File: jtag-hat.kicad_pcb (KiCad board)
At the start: 2 copper layers, 65 x 56 mm, 18 parts, among them J1 I2C header, J10 ARM-20 JTAG, J2 RPi_GPIO, J3 RPI UART, J4 UART IN, J5 JTAG 2x4, SW1 SW_Push

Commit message: v1.3
- Swapped the JTAG connector placements for connecting convenience
- Changed resistors to 0402
- Removed silkscreen around unused PI-header holes
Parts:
- R1, R2, R3, R4, R5: footprint Resistor_SMD:R_0805_2012Metric_Pad1.20x1.40mm_HandSolder -> Resistor_SMD:R_0402_1005Metric_Pad0.72x0.64mm_HandSolder
- moved J5 29.3 mm to (163.2, 81.4)
- moved J10 13.6 mm to (153.6, 80.0)
- moved R2 5.31 mm to (156.7, 67.0), turned to -90 degrees
- moved R5 4.57 mm to (154.4, 67.0)
- moved R3 2.38 mm to (153.7, 64.0), turned to 90 degrees
- moved R4 1.32 mm to (151.3, 64.0)
- moved G*** 0.18 mm to (113.4, 96.3)
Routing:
- net /RPi_GPIO/TRST: track 67.1 -> 50.9 mm
- net /RPi_GPIO/TDI: track 68.1 -> 53.0 mm, vias 0 -> 1
- net /RPi_GPIO/TCK: track 55.7 -> 40.9 mm
- net /RPi_GPIO/RXD5: track 4.38 -> 11.4 mm
- net /RPi_GPIO/TDO: track 48.1 -> 54.9 mm
- net /RPi_GPIO/PIN6_RXTX: track 11.6 -> 17.6 mm, vias 0 -> 2
- net /RPi_GPIO/SRST: track 30.7 -> 25.1 mm
- net /RPi_GPIO/PIN4_RXTX: track 20.0 -> 14.9 mm
- net /RPi_GPIO/TXD5: track 7.08 -> 10.9 mm
- net GND: track 118.8 -> 115.5 mm, vias 0 -> 1
- net /RPi_GPIO/TMS: track 58.5 -> 56.2 mm
- net /RPi_GPIO/GPIO23: track 71.5 -> 73.6 mm, vias 0 -> 1
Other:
- board text added: "JTAG HAT + Shutdown v1.3"
- board text removed: "JTAG HAT + Shutdown v1.2"

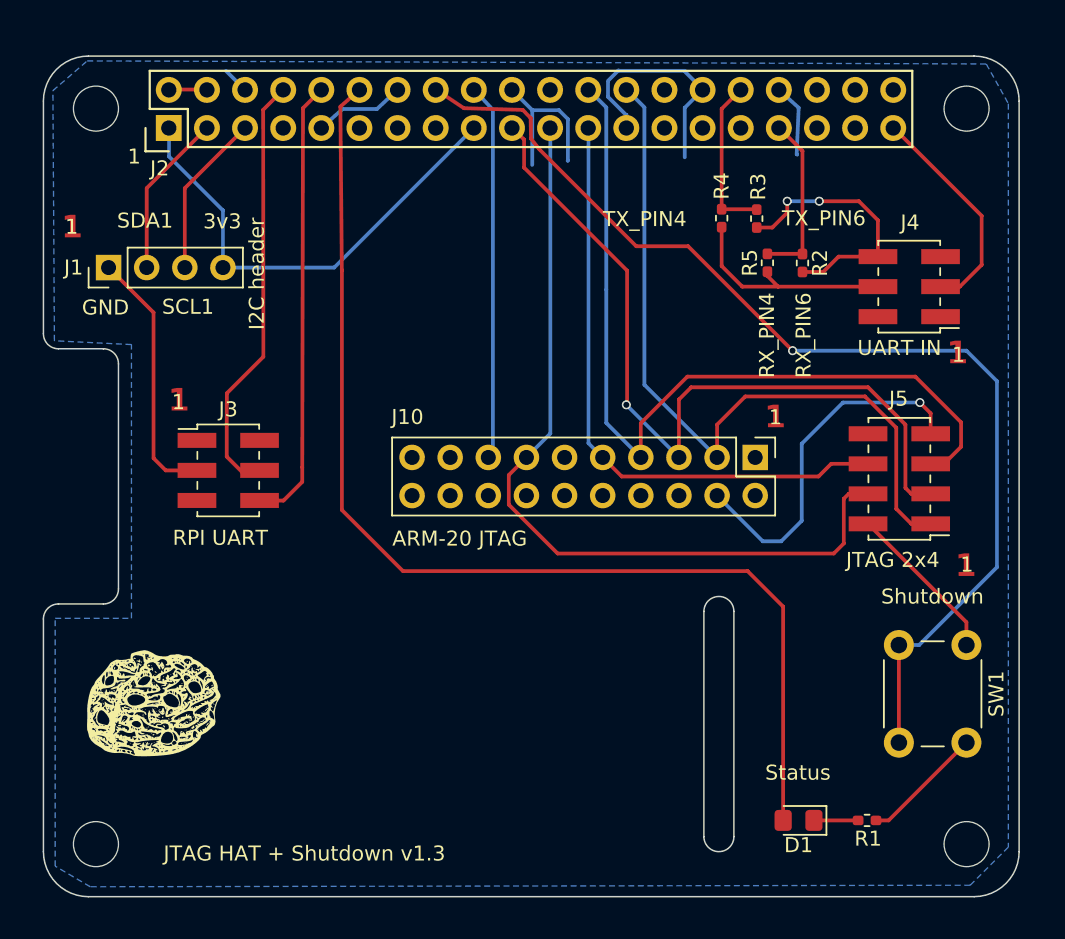
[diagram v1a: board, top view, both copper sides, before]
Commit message: v1.4
    - Rotate rpi uart header
    - Add second status led
    - Minor cleanup
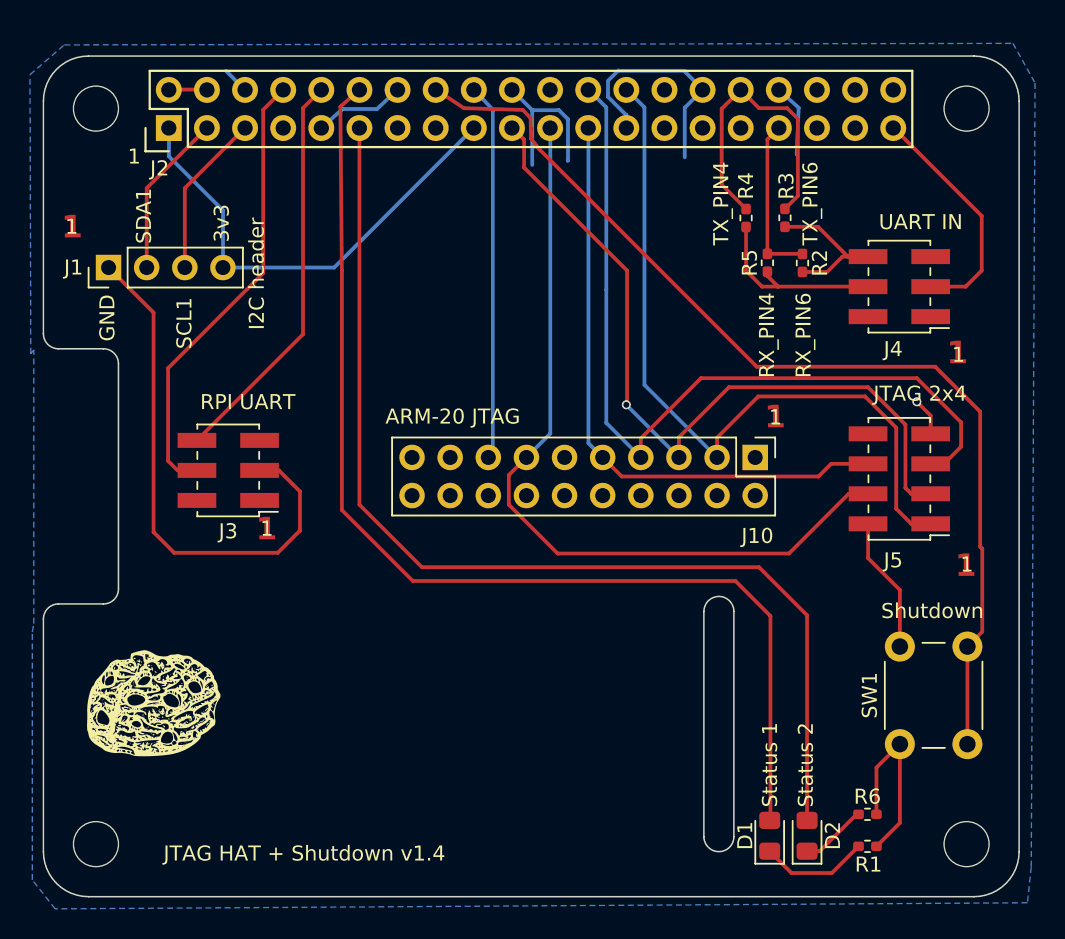
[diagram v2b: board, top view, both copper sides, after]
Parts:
- added D2: LED, LED_SMD:LED_0805_2012Metric_Pad1.15x1.40mm_HandSolder, F.Cu at (157.0, 105.2)
- added R6: R2200, Resistor_SMD:R_0402_1005Metric_Pad0.72x0.64mm_HandSolder, F.Cu at (161.0, 103.7)
- moved SW1 7.95 mm to (163.2, 99.1), turned to 90 degrees
- moved D1 2.18 mm to (154.5, 105.2), turned to 90 degrees
- moved R3 1.88 mm to (155.5, 64.0)
- moved R1 1.73 mm to (161.0, 105.9)
- moved R4 1.63 mm to (153.0, 64.0)
- moved J4 0.66 mm to (163.2, 68.6)
- turned J3 to 180 degrees
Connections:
- J2 pad 11: unconnected-(J2-BCM17-Pad11) -> /RPi_GPIO/GPIO17
- J5 pad 8: unconnected-(J5-Pin_8-Pad8) -> /RPi_GPIO/VCC-NC
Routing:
- net /RPi_GPIO/GPIO17: track 0.00 -> 71.6 mm
- net /RPi_GPIO/TXD5: track 10.9 -> 20.1 mm
- net /RPi_GPIO/PIN6_RXTX: track 17.6 -> 11.2 mm, vias 2 -> 0
- net /RPi_GPIO/GPIO23: track 73.6 -> 68.4 mm, vias 1 -> 0
- net Net-(D2-K): track 0.00 -> 4.45 mm
- net Net-(D1-K): track 2.94 -> 7.26 mm
- net /RPi_GPIO/RXD0: track 29.9 -> 26.8 mm
- net /RPi_GPIO/PIN4_RXTX: track 14.9 -> 12.8 mm
- net /RPi_GPIO/TDO: track 54.9 -> 53.2 mm
- net /RPi_GPIO/TXD0: track 28.6 -> 30.1 mm
- net /RPi_GPIO/TDI: track 53.0 -> 51.5 mm
- net /RPi_GPIO/GPIO18: track 74.9 -> 73.7 mm
- net /RPi_GPIO/TMS: track 56.2 -> 55.6 mm
- net /RPi_GPIO/TRST: track 50.9 -> 50.4 mm
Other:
- board text added: "JTAG HAT + Shutdown v1.4"
- board text added: "Status 1"
- board text added: "Status 2"
- board text removed: "JTAG HAT + Shutdown v1.3"
- board text removed: "Status"

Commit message: v1.5
- Changed mounting holes to 3.2mm (for M3)
- Swapped Pi-header for a straight pin-header
- Converted schematic from sub-schematic
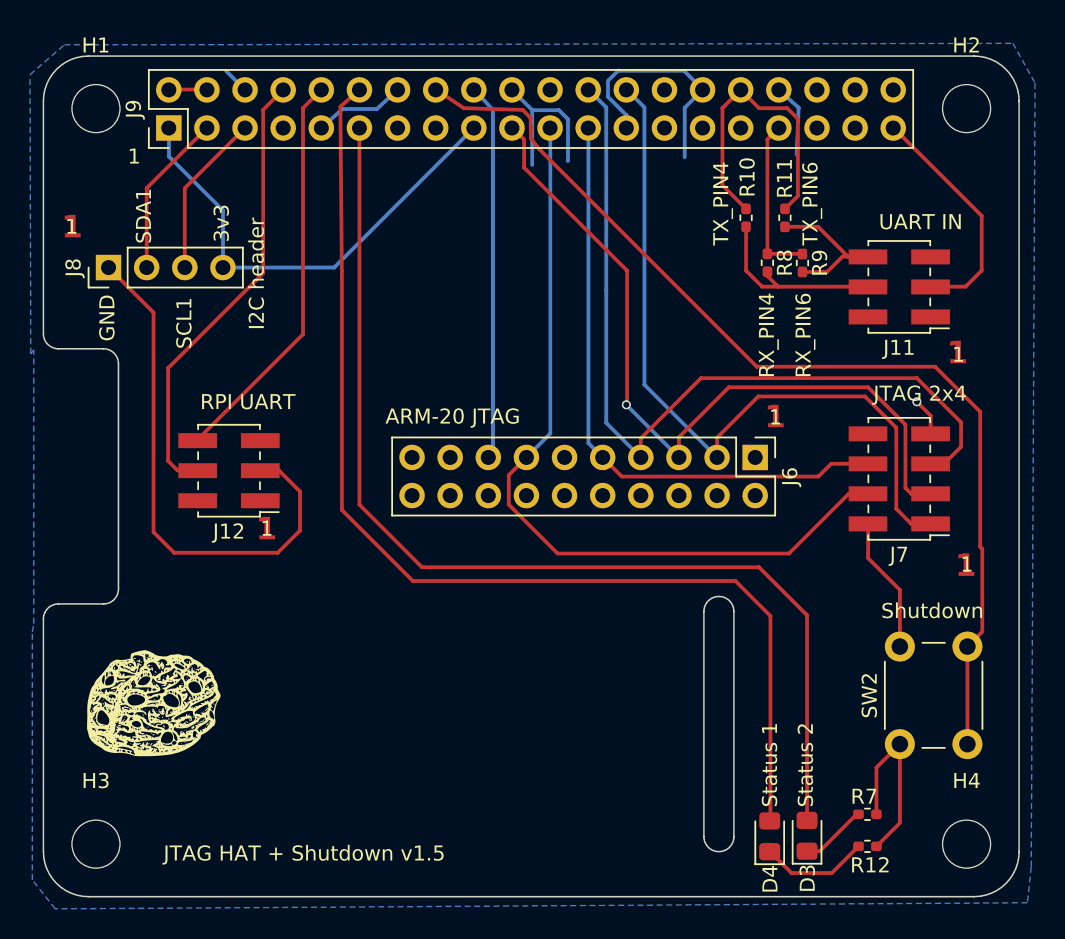
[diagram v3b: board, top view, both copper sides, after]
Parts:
- removed D1, D2: LED, LED_SMD:LED_0805_2012Metric_Pad1.15x1.40mm_HandSolder
- removed J1: I2C header, Connector_PinHeader_2.54mm:PinHeader_1x04_P2.54mm_Vertical
- removed J10: ARM-20 JTAG, Connector_PinHeader_2.54mm:PinHeader_2x10_P2.54mm_Vertical
- removed J2: RPi_GPIO, RPi_Hat:Pin_Header_Straight_2x20
- removed J3: RPI UART, Connector_PinHeader_2.00mm:PinHeader_2x03_P2.00mm_Vertical_SMD
- removed J4: UART IN, Connector_PinHeader_2.00mm:PinHeader_2x03_P2.00mm_Vertical_SMD
- removed J5: JTAG 2x4, Connector_PinHeader_2.00mm:PinHeader_2x04_P2.00mm_Vertical_SMD
- removed R1, R6: R2200, Resistor_SMD:R_0402_1005Metric_Pad0.72x0.64mm_HandSolder
- removed R2, R3, R4, R5: R0, Resistor_SMD:R_0402_1005Metric_Pad0.72x0.64mm_HandSolder
- removed SW1: SW_Push, Button_Switch_THT:SW_PUSH_6mm
- added D3: LED, LED_SMD:LED_0805_2012Metric_Pad1.15x1.40mm_HandSolder, F.Cu at (157.0, 105.2)
- added D4: LED, LED_SMD:LED_0805_2012Metric_Pad1.15x1.40mm_HandSolder, F.Cu at (154.5, 105.2)
- added J11: UART IN, Connector_PinHeader_2.00mm:PinHeader_2x03_P2.00mm_Vertical_SMD, F.Cu at (163.2, 68.6)
- added J12: RPI UART, Connector_PinHeader_2.00mm:PinHeader_2x03_P2.00mm_Vertical_SMD, F.Cu at (118.5, 80.8)
- added J6: ARM-20 JTAG, Connector_PinHeader_2.54mm:PinHeader_2x10_P2.54mm_Vertical, F.Cu at (153.6, 80.0)
- added J7: JTAG 2x4, Connector_PinHeader_2.00mm:PinHeader_2x04_P2.00mm_Vertical_SMD, F.Cu at (163.2, 81.4)
- added J8: I2C header, Connector_PinHeader_2.54mm:PinHeader_1x04_P2.54mm_Vertical, F.Cu at (110.5, 67.3)
- added J9: RPi_GPIO, Connector_PinHeader_2.54mm:PinHeader_2x20_P2.54mm_Vertical, F.Cu at (114.5, 58.0)
- added R10: R0, Resistor_SMD:R_0402_1005Metric_Pad0.72x0.64mm_HandSolder, F.Cu at (153.0, 64.0)
- added R11: R0, Resistor_SMD:R_0402_1005Metric_Pad0.72x0.64mm_HandSolder, F.Cu at (155.5, 64.0)
- added R12: R2200, Resistor_SMD:R_0402_1005Metric_Pad0.72x0.64mm_HandSolder, F.Cu at (161.0, 105.9)
- added R7: R2200, Resistor_SMD:R_0402_1005Metric_Pad0.72x0.64mm_HandSolder, F.Cu at (161.0, 103.7)
- added R8: R0, Resistor_SMD:R_0402_1005Metric_Pad0.72x0.64mm_HandSolder, F.Cu at (154.4, 67.0)
- added R9: R0, Resistor_SMD:R_0402_1005Metric_Pad0.72x0.64mm_HandSolder, F.Cu at (156.7, 67.0)
- added SW2: SW_Push, Button_Switch_THT:SW_PUSH_6mm, F.Cu at (163.2, 99.1)
- H1, H2, H3, H4: footprint MountingHole:MountingHole_3mm -> MountingHole:MountingHole_3.2mm_M3
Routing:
- net /RPi_GPIO/GPIO18: track 73.7 -> 0.00 mm
- net /GPIO18: track 0.00 -> 73.7 mm
- net /RPi_GPIO/GPIO17: track 71.6 -> 0.00 mm
- net /GPIO17: track 0.00 -> 71.6 mm
- net /RPi_GPIO/GPIO23: track 68.4 -> 0.00 mm
- net /GPIO23: track 0.00 -> 68.4 mm
- net /TMS: track 0.00 -> 55.6 mm
- net /RPi_GPIO/TMS: track 55.6 -> 0.00 mm
- net /TDO: track 0.00 -> 53.2 mm
- net /RPi_GPIO/TDO: track 53.2 -> 0.00 mm
- net /TDI: track 0.00 -> 51.5 mm, vias 0 -> 1
- net /RPi_GPIO/TDI: track 51.5 -> 0.00 mm, vias 1 -> 0
- net /TRST: track 0.00 -> 50.4 mm
- net /RPi_GPIO/TRST: track 50.4 -> 0.00 mm
- net /TCK: track 0.00 -> 40.9 mm
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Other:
- board text added: "JTAG HAT + Shutdown v1.5"
- board text removed: "JTAG HAT + Shutdown v1.4"
